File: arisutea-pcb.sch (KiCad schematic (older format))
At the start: 45 parts, among them J10 PF6, J11 PF7, J12 VCC, J13 D+, J14 D-, J15 GND, J2 MISO, J3 VCC, J4 SCK, J5 MOSI, J6 RES, J7 GND, J8 PF4, J9 PF5, U1 USBLC6-2SC6, U2 ATmega32U4-AU, Y1 Crystal_GND24

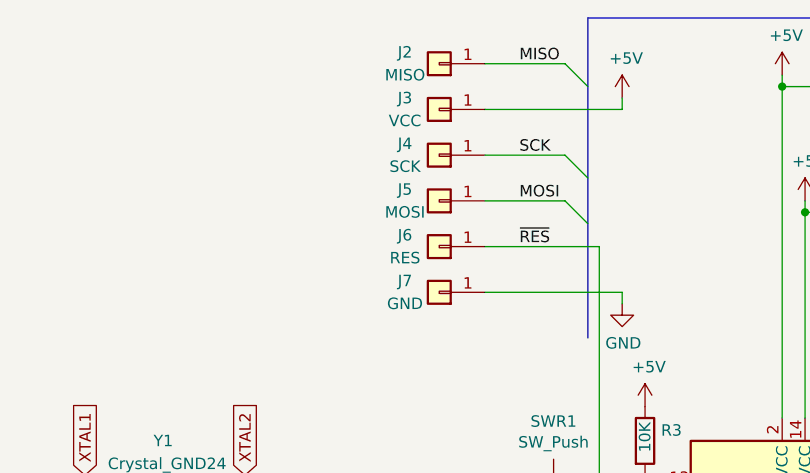
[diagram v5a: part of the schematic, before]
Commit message: 0.5 update
Fixes some routing that really did not need to be fixed but my OCD was screaming at me. Fixes an issue with the USB port only being shown as a through hole component and not an SMD. Reup gerbies, BOM and POS files.
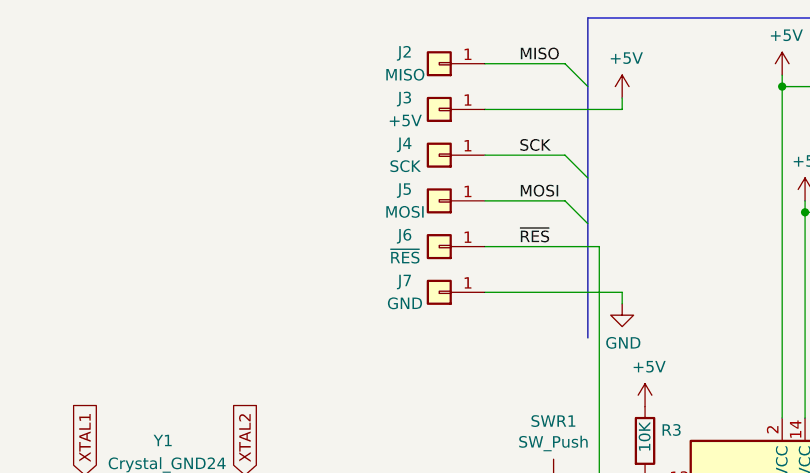
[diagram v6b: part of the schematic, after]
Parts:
- J3: value VCC -> +5V
- J6: value RES -> ~RES~
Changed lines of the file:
@@
 encoding utf-8
 Sheet 1 2
-Title "Arisutea"
-Date ""
-Rev "0.4"
-Comp "3x6 Designs"
+Title "Arisutea Keyboard"
+Date "2021-03-25"
+Rev "0.5"
+Comp "3x6 Design"
 Comment1 ""
 Comment2 ""
@@
 P 3350 1700
 F 0 "J6" H 3500 1650 50  0000 C CNN
-F 1 "RES" H 3500 1750 50  0000 C CNN
+F 1 "~RES~" H 3500 1750 50  0000 C CNN
 F 2 "arisutea:PinHeader_1x01_P2.54mm_Vertical" H 3350 1700 50  0001 C CNN
 F 3 "~" H 3350 1700 50  0001 C CNN
@@
 P 3350 1100
 F 0 "J3" H 3500 1050 50  0000 C CNN
-F 1 "VCC" H 3500 1150 50  0000 C CNN
+F 1 "+5V" H 3500 1150 50  0000 C CNN
 F 2 "arisutea:PinHeader_1x01_P2.54mm_Vertical" H 3350 1100 50  0001 C CNN
 F 3 "~" H 3350 1100 50  0001 C CNN
@@
 	1    3350 900
 	-1   0    0    1
+$EndComp
+$Comp
+L arisutea-pcb-r1:arisutea_logo LOGO2
+U 1 1 605B7585
+P 10250 6150
+F 0 "LOGO2" H 10250 6350 50  0000 C CNN
+F 1 "arisutea_logo" H 10325 6524 50  0001 C CNN
+F 2 "arisutea:arisutea_logo" H 10250 6500 50  0001 C CNN
+F 3 "" H 10250 6500 50  0001 C CNN
+	1    10250 6150
+	1    0    0    -1
 $EndComp
 Wire Bus Line
@@
 Wire Bus Line
 	7200 2750 7200 5800
-$Comp
-L arisutea-pcb-r1:arisutea_logo LOGO2
-U 1 1 605B7585
-P 10250 6150
-F 0 "LOGO2" H 10250 6350 50  0000 C CNN
-F 1 "arisutea_logo" H 10325 6524 50  0001 C CNN
-F 2 "arisutea:arisutea_logo" H 10250 6500 50  0001 C CNN
-F 3 "" H 10250 6500 50  0001 C CNN
-	1    10250 6150
-	1    0    0    -1
-$EndComp
 $EndSCHEMATC

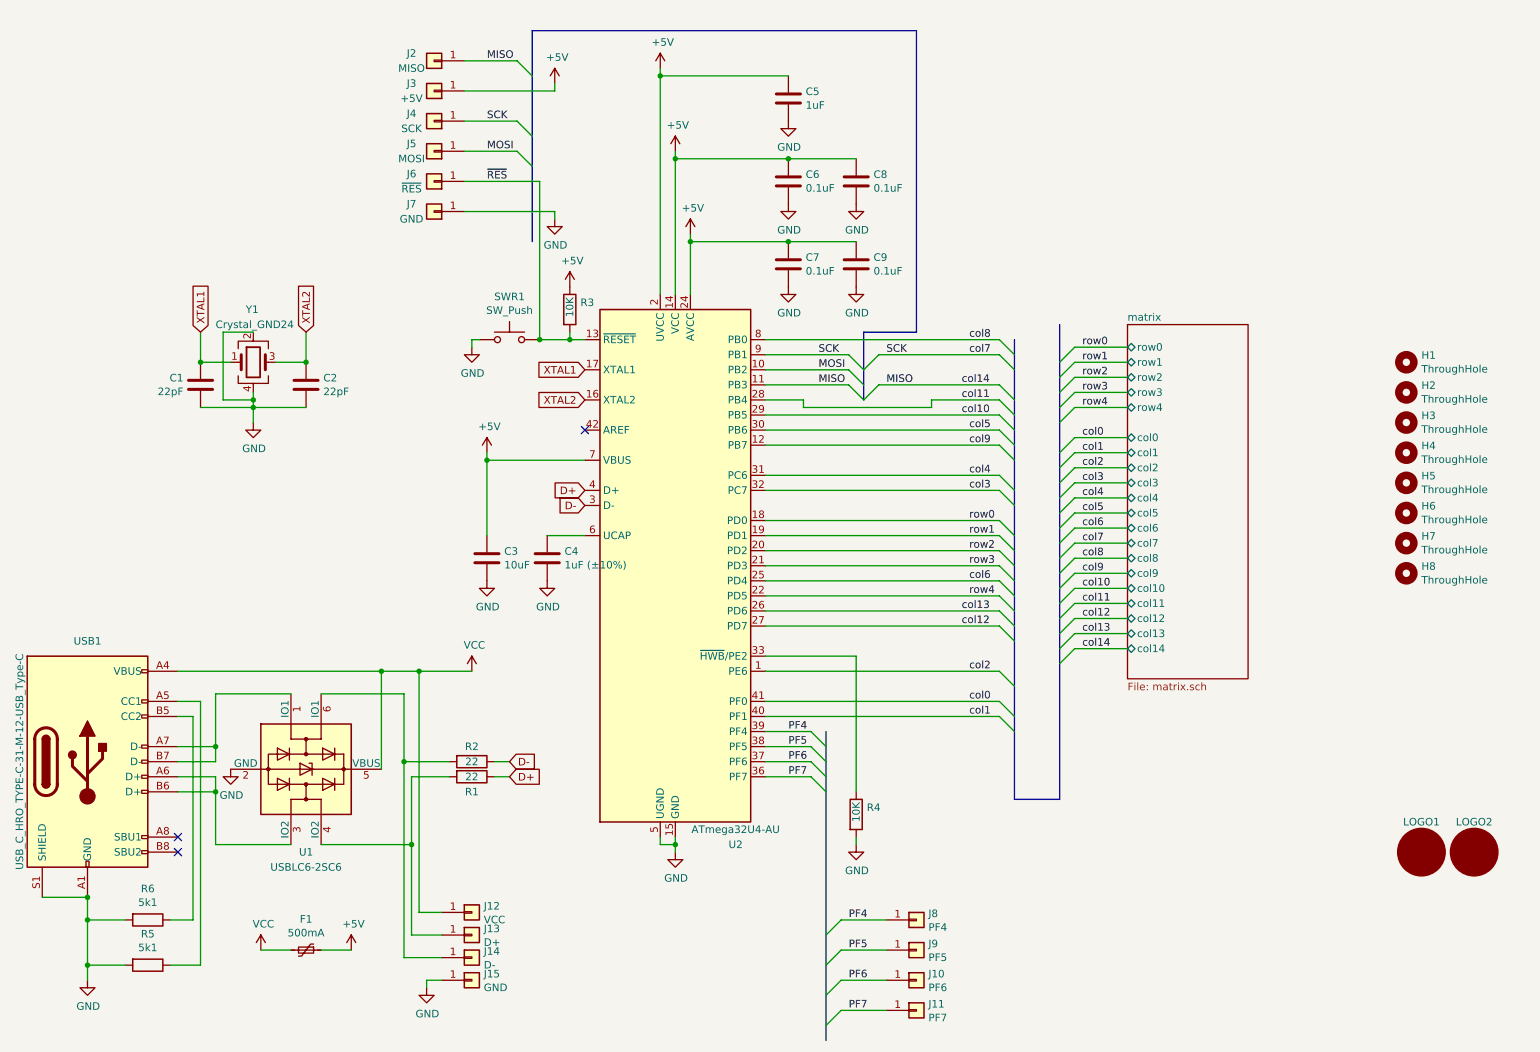
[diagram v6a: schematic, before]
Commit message: added LED strip and indicator support, new cases for indicators
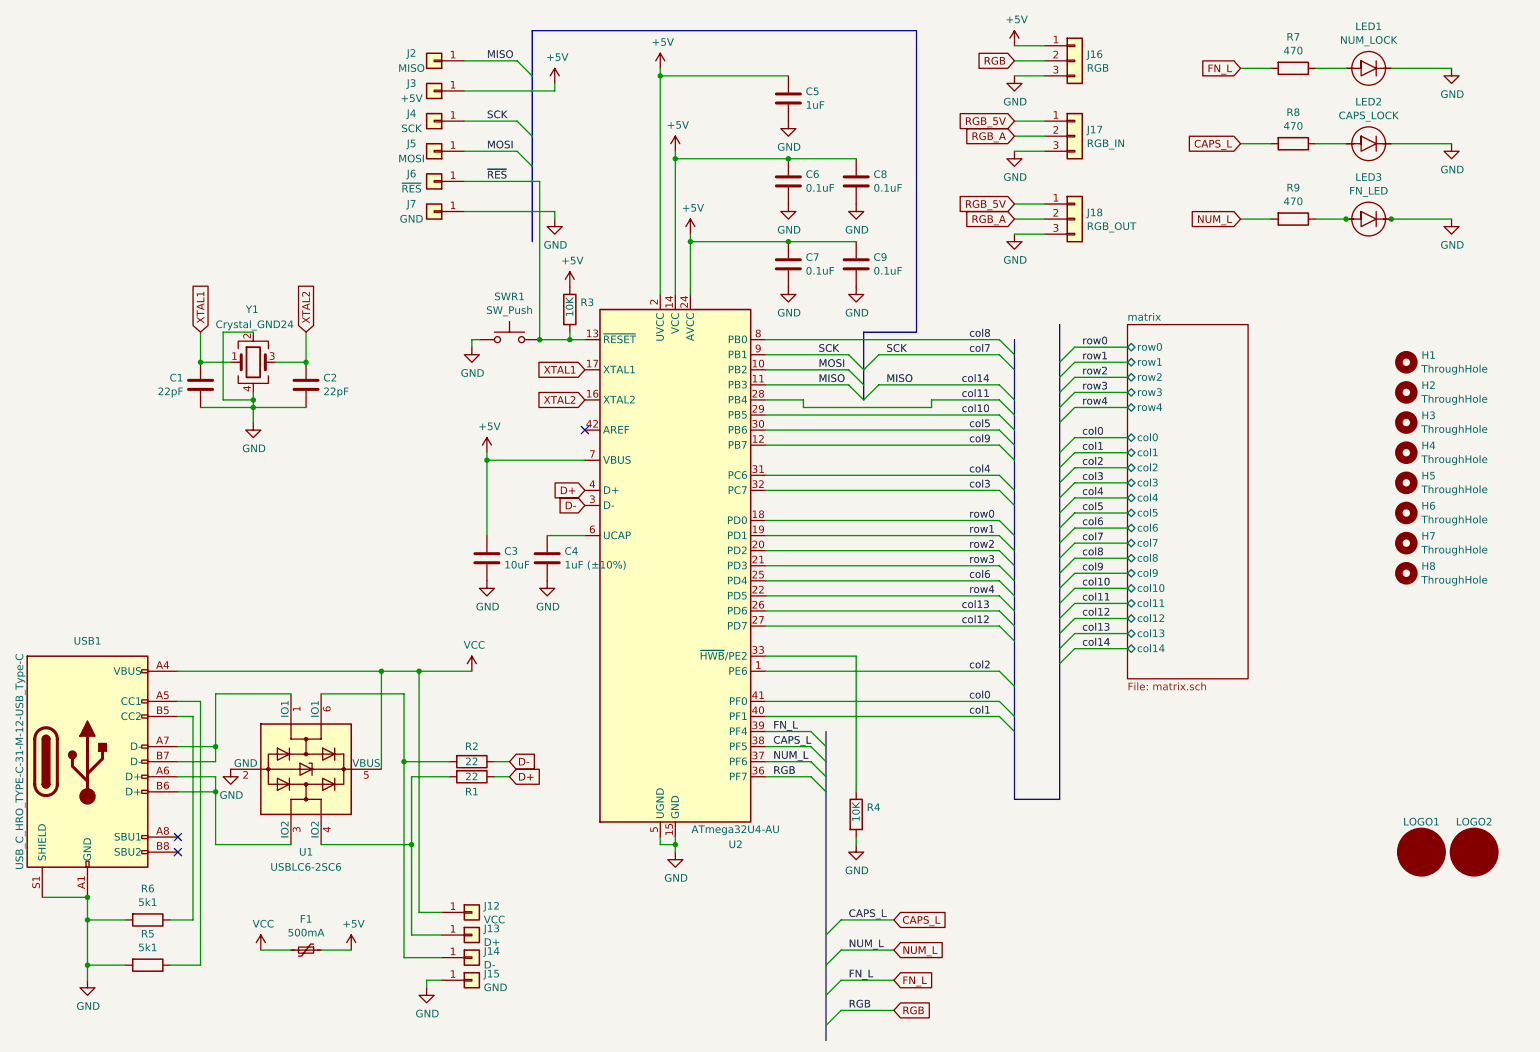
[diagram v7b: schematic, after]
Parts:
- removed J10: PF6, arisutea:PinHeader_1x01_P2.54mm_Vertical, symbol Connector_Generic:Conn_01x01
- removed J11: PF7, arisutea:PinHeader_1x01_P2.54mm_Vertical, symbol Connector_Generic:Conn_01x01
- removed J8: PF4, arisutea:PinHeader_1x01_P2.54mm_Vertical, symbol Connector_Generic:Conn_01x01
- removed J9: PF5, arisutea:PinHeader_1x01_P2.54mm_Vertical, symbol Connector_Generic:Conn_01x01
- added J16: RGB, arisutea:PinHeader_1x03_P2.54mm_Vertical, symbol Connector_Generic:Conn_01x03
- added J17: RGB_IN, arisutea:PinHeader_1x03_P2.54mm_Vertical, symbol Connector_Generic:Conn_01x03
- added J18: RGB_OUT, arisutea:PinHeader_1x03_P2.54mm_Vertical, symbol Connector_Generic:Conn_01x03
- added LED1: NUM_LOCK, arisutea:LED_IN-S124ARUW, symbol arisutea-pcb-r1:LED
- added LED2: CAPS_LOCK, arisutea:LED_IN-S124ARUW, symbol arisutea-pcb-r1:LED
- added LED3: FN_LED, arisutea:LED_IN-S124ARUW, symbol arisutea-pcb-r1:LED
- added R7, R8, R9: 470, arisutea:R_0805_2012Metric_Pad1.20x1.40mm_HandSolder, symbol Device:R
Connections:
- net +5V: now also J16.1 (Pin_1)
- net GND: now also J16.3 (Pin_3), J17.3 (Pin_3), J18.3 (Pin_3), LED1.C, LED2.C, LED3.C
- net PF4 renamed FN_L
- net FN_L: now also R7.2
- net PF5 renamed CAPS_L
- net CAPS_L: now also R8.2
- net PF6 renamed NUM_L
- net NUM_L: now also R9.2
- net PF7 renamed RGB
- net RGB: now also J16.2 (Pin_2)
- new net: LED3.A, R9.1
- new net: LED2.A, R8.1
- new net: LED1.A, R7.1
- new net RGB_5V: J17.1 (Pin_1), J18.1 (Pin_1)
- new net RGB_A: J17.2 (Pin_2), J18.2 (Pin_2)

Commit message: add firmware files
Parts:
- added LOGO3, LOGO4: arisutea_logo, Symbol:OSHW-Logo_5.7x6mm_SilkScreen, symbol arisutea-pcb-r1:arisutea_logo
- added LOGO5, LOGO6: arisutea_logo, arisutea:arisutea_logo, symbol arisutea-pcb-r1:arisutea_logo
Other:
- moved on the sheet: LOGO1, LOGO2
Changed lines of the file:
@@
 	7600 3400 7950 3400
 Entry Wire Line
-	5950 7300 6050 7200
-Entry Wire Line
-	5950 7100 6050 7000
+	5950 7000 6050 6900
 Entry Wire Line
 	5950 6900 6050 6800
+Entry Wire Line
+	5950 6800 6050 6700
 Entry Wire Line
 	5950 6700 6050 6600
@@
 Text Label 6100 6600 0    50   ~ 0
 CAPS_L
+Text Label 6100 6700 0    50   ~ 0
+NUM_L
 Text Label 6100 6800 0    50   ~ 0
-NUM_L
-Text Label 6100 7000 0    50   ~ 0
 FN_L
-Text Label 6100 7200 0    50   ~ 0
+Text Label 6100 6900 0    50   ~ 0
 RGB
 NoConn ~ 4350 3350
@@
 U 1 1 5F98F744
 P 1450 6900
-F 0 "R5" V 1243 6900 50  0000 C CNN
-F 1 "5k1" V 1334 6900 50  0000 C CNN
+F 0 "R5" V 1350 6900 50  0000 C CNN
+F 1 "5k1" V 1450 6900 50  0000 C CNN
 F 2 "arisutea:R_0805_2012Metric_Pad1.20x1.40mm_HandSolder" V 1380 6900 50  0001 C CNN
 F 3 "~" H 1450 6900 50  0001 C CNN
@@
 U 1 1 5F9A4013
 P 1450 6600
-F 0 "R6" V 1243 6600 50  0000 C CNN
-F 1 "5k1" V 1334 6600 50  0000 C CNN
+F 0 "R6" V 1350 6600 50  0000 C CNN
+F 1 "5k1" V 1450 6600 50  0000 C CNN
 F 2 "arisutea:R_0805_2012Metric_Pad1.20x1.40mm_HandSolder" V 1380 6600 50  0001 C CNN
 F 3 "~" H 1450 6600 50  0001 C CNN
@@
 L arisutea-pcb-r1:arisutea_logo LOGO1
 U 1 1 6042E29E
-P 9900 6150
-F 0 "LOGO1" H 9900 6350 50  0000 C CNN
-F 1 "arisutea_logo" H 9975 6524 50  0001 C CNN
-F 2 "arisutea:arisutea_logo" H 9900 6500 50  0001 C CNN
-F 3 "" H 9900 6500 50  0001 C CNN
-	1    9900 6150
+P 8700 6100
+F 0 "LOGO1" H 8700 6300 50  0000 C CNN
+F 1 "arisutea_logo" H 8775 6474 50  0001 C CNN
+F 2 "arisutea:arisutea_logo" H 8700 6450 50  0001 C CNN
+F 3 "" H 8700 6450 50  0001 C CNN
+	1    8700 6100
 	1    0    0    -1
 $EndComp
@@
 L arisutea-pcb-r1:arisutea_logo LOGO2
 U 1 1 605B7585
-P 10250 6150
-F 0 "LOGO2" H 10250 6350 50  0000 C CNN
-F 1 "arisutea_logo" H 10325 6524 50  0001 C CNN
-F 2 "arisutea:arisutea_logo" H 10250 6500 50  0001 C CNN
-F 3 "" H 10250 6500 50  0001 C CNN
-	1    10250 6150
+P 9050 6100
+F 0 "LOGO2" H 9050 6300 50  0000 C CNN
+F 1 "arisutea_logo" H 9125 6474 50  0001 C CNN
+F 2 "arisutea:arisutea_logo" H 9050 6450 50  0001 C CNN
+F 3 "" H 9050 6450 50  0001 C CNN
+	1    9050 6100
 	1    0    0    -1
 $EndComp
@@
 Wire Wire Line
 	7200 1950 7400 1950
-Text GLabel 6400 7200 2    50   Input ~ 0
+Text GLabel 6400 6900 2    50   Input ~ 0
 RGB
 Text Label 5600 5450 0    50   ~ 0
 CAPS_L
-Text GLabel 6400 7000 2    50   Input ~ 0
+Text GLabel 6400 6800 2    50   Input ~ 0
 FN_L
-Text GLabel 6400 6800 2    50   Input ~ 0
+Text GLabel 6400 6700 2    50   Input ~ 0
 NUM_L
 Text GLabel 6400 6600 2    50   Input ~ 0
@@
 	6050 6600 6400 6600
 Wire Wire Line
+	6050 6700 6400 6700
+Wire Wire Line
 	6050 6800 6400 6800
 Wire Wire Line
-	6050 7000 6400 7000
-Wire Wire Line
-	6050 7200 6400 7200
+	6050 6900 6400 6900
 $Comp
 L arisutea-pcb-r1:LED LED3
@@
 U 1 1 60669F17
 P 9050 1450
-F 0 "R8" V 8843 1450 50  0000 C CNN
-F 1 "470" V 8934 1450 50  0000 C CNN
+F 0 "R8" V 8950 1450 50  0000 C CNN
+F 1 "470" V 9050 1450 50  0000 C CNN
 F 2 "arisutea:R_0805_2012Metric_Pad1.20x1.40mm_HandSolder" V 8980 1450 50  0001 C CNN
 F 3 "~" H 9050 1450 50  0001 C CNN
@@
 U 1 1 6066AD99
 P 9050 1950
-F 0 "R9" V 8843 1950 50  0000 C CNN
-F 1 "470" V 8934 1950 50  0000 C CNN
+F 0 "R9" V 8950 1950 50  0000 C CNN
+F 1 "470" V 9050 1950 50  0000 C CNN
 F 2 "arisutea:R_0805_2012Metric_Pad1.20x1.40mm_HandSolder" V 8980 1950 50  0001 C CNN
 F 3 "~" H 9050 1950 50  0001 C CNN
@@
 U 1 1 6066B154
 P 9050 950
-F 0 "R7" V 8843 950 50  0000 C CNN
-F 1 "470" V 8934 950 50  0000 C CNN
+F 0 "R7" V 8950 950 50  0000 C CNN
+F 1 "470" V 9050 950 50  0000 C CNN
 F 2 "arisutea:R_0805_2012Metric_Pad1.20x1.40mm_HandSolder" V 8980 950 50  0001 C CNN
 F 3 "~" H 9050 950 50  0001 C CNN
@@
 Text GLabel 8700 950  0    50   Input ~ 0
 FN_L
+$Comp
+L arisutea-pcb-r1:arisutea_logo LOGO3
+U 1 1 6062F214
+P 9400 6100
+F 0 "LOGO3" H 9400 6300 50  0000 C CNN
+F 1 "arisutea_logo" H 9475 6474 50  0001 C CNN
+F 2 "Symbol:OSHW-Logo_5.7x6mm_SilkScreen" H 9400 6450 50  0001 C CNN
+F 3 "" H 9400 6450 50  0001 C CNN
+	1    9400 6100
+	1    0    0    -1
+$EndComp
+$Comp
+L arisutea-pcb-r1:arisutea_logo LOGO4
+U 1 1 6062F624
+P 9750 6100
+F 0 "LOGO4" H 9750 6300 50  0000 C CNN
+F 1 "arisutea_logo" H 9825 6474 50  0001 C CNN
+F 2 "Symbol:OSHW-Logo_5.7x6mm_SilkScreen" H 9750 6450 50  0001 C CNN
+F 3 "" H 9750 6450 50  0001 C CNN
+	1    9750 6100
+	1    0    0    -1
+$EndComp
+$Comp
+L arisutea-pcb-r1:arisutea_logo LOGO5
+U 1 1 6063AB78
+P 10100 6100
+F 0 "LOGO5" H 10100 6300 50  0000 C CNN
+F 1 "arisutea_logo" H 10175 6474 50  0001 C CNN
+F 2 "arisutea:arisutea_logo" H 10100 6450 50  0001 C CNN
+F 3 "" H 10100 6450 50  0001 C CNN
+	1    10100 6100
+	1    0    0    -1
+$EndComp
+$Comp
+L arisutea-pcb-r1:arisutea_logo LOGO6
+U 1 1 6063AEC9
+P 10450 6100
+F 0 "LOGO6" H 10450 6300 50  0000 C CNN
+F 1 "arisutea_logo" H 10525 6474 50  0001 C CNN
+F 2 "arisutea:arisutea_logo" H 10450 6450 50  0001 C CNN
+F 3 "" H 10450 6450 50  0001 C CNN
+	1    10450 6100
+	1    0    0    -1
+$EndComp
 Wire Bus Line
 	6200 2700 6200 3150
@@
 	4000 700  4000 2100
 Wire Bus Line
-	5950 5350 5950 7400
+	5950 5350 5950 7100
 Wire Bus Line
 	7500 2650 7500 5800
 Wire Bus Line
 	7200 2750 7200 5800
-Connection ~ 9400 1950
-Connection ~ 9700 1950
 $EndSCHEMATC
